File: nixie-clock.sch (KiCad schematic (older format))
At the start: 7 parts

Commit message: Wyprowadzenie VDD (3,3V); komentarze
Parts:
- U?: value STM32F103CBTx -> STM32F103CBT6
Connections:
- net labels added: VDD
- wire segments 13 -> 28
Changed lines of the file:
@@
 P 6000 3850
 F 0 "U?" H 3200 5575 50  0000 L BNN
-F 1 "STM32F103CBTx" H 8800 5575 50  0000 R BNN
+F 1 "STM32F103CBT6" H 8800 5575 50  0000 R BNN
 F 2 "LQFP48" H 8800 5525 50  0000 R TNN
 F 3 "" H 6000 3850 50  0000 C CNN
@@
 	1100 3100 1100 3200
 $Sheet
-S 600  600  950  1000
+S 600  750  850  800
 U 5814F4D4
 F0 "Power supply" 60
 F1 "power-supply.sch" 60
+F2 "VDD" O R 1450 850 60
+F3 "GND" O R 1450 1150 60
+F4 "200VDC" O R 1450 1300 60
+F5 "200VGND" O R 1450 1450 60
+F6 "5VDC" O R 1450 1000 60
 $EndSheet
+$Comp
+L PWR_FLAG #FLG?
+U 1 1 581749DC
+P 1800 700
+F 0 "#FLG?" H 1800 795 50  0001 C CNN
+F 1 "PWR_FLAG" H 1800 880 50  0000 C CNN
+F 2 "" H 1800 700 50  0000 C CNN
+F 3 "" H 1800 700 50  0000 C CNN
+	1    1800 700
+	1    0    0    -1
+$EndComp
+$Comp
+L PWR_FLAG #FLG?
+U 1 1 58174A1B
+P 2250 700
+F 0 "#FLG?" H 2250 795 50  0001 C CNN
+F 1 "PWR_FLAG" H 2250 880 50  0000 C CNN
+F 2 "" H 2250 700 50  0000 C CNN
+F 3 "" H 2250 700 50  0000 C CNN
+	1    2250 700
+	1    0    0    -1
+$EndComp
+Wire Wire Line
+	2250 700  2250 1150
+Wire Wire Line
+	1800 700  1800 850
+Connection ~ 1800 850
+Wire Wire Line
+	2250 1150 1450 1150
+Wire Wire Line
+	1100 2000 1100 2150
+Wire Wire Line
+	1800 850  1450 850
+Text Label 1650 850  2    60   ~ 0
+VDD
+Text Label 1650 1150 2    60   ~ 0
+GND
+Wire Wire Line
+	5600 1900 6100 1900
+Wire Wire Line
+	5800 1900 5800 2050
+Wire Wire Line
+	5900 1900 5900 2050
+Connection ~ 5800 1900
+Wire Wire Line
+	6000 1900 6000 2050
+Connection ~ 5900 1900
+Wire Wire Line
+	6100 1900 6100 2050
+Connection ~ 6000 1900
+Text Label 5750 1900 2    60   ~ 0
+VDD
+Wire Wire Line
+	5600 5800 6100 5800
+Wire Wire Line
+	5800 5800 5800 5650
+Wire Wire Line
+	5900 5800 5900 5650
+Connection ~ 5800 5800
+Wire Wire Line
+	6000 5800 6000 5650
+Connection ~ 5900 5800
+Wire Wire Line
+	6100 5800 6100 5650
+Connection ~ 6000 5800
+Text Label 5750 5800 2    60   ~ 0
+VDD
 $EndSCHEMATC

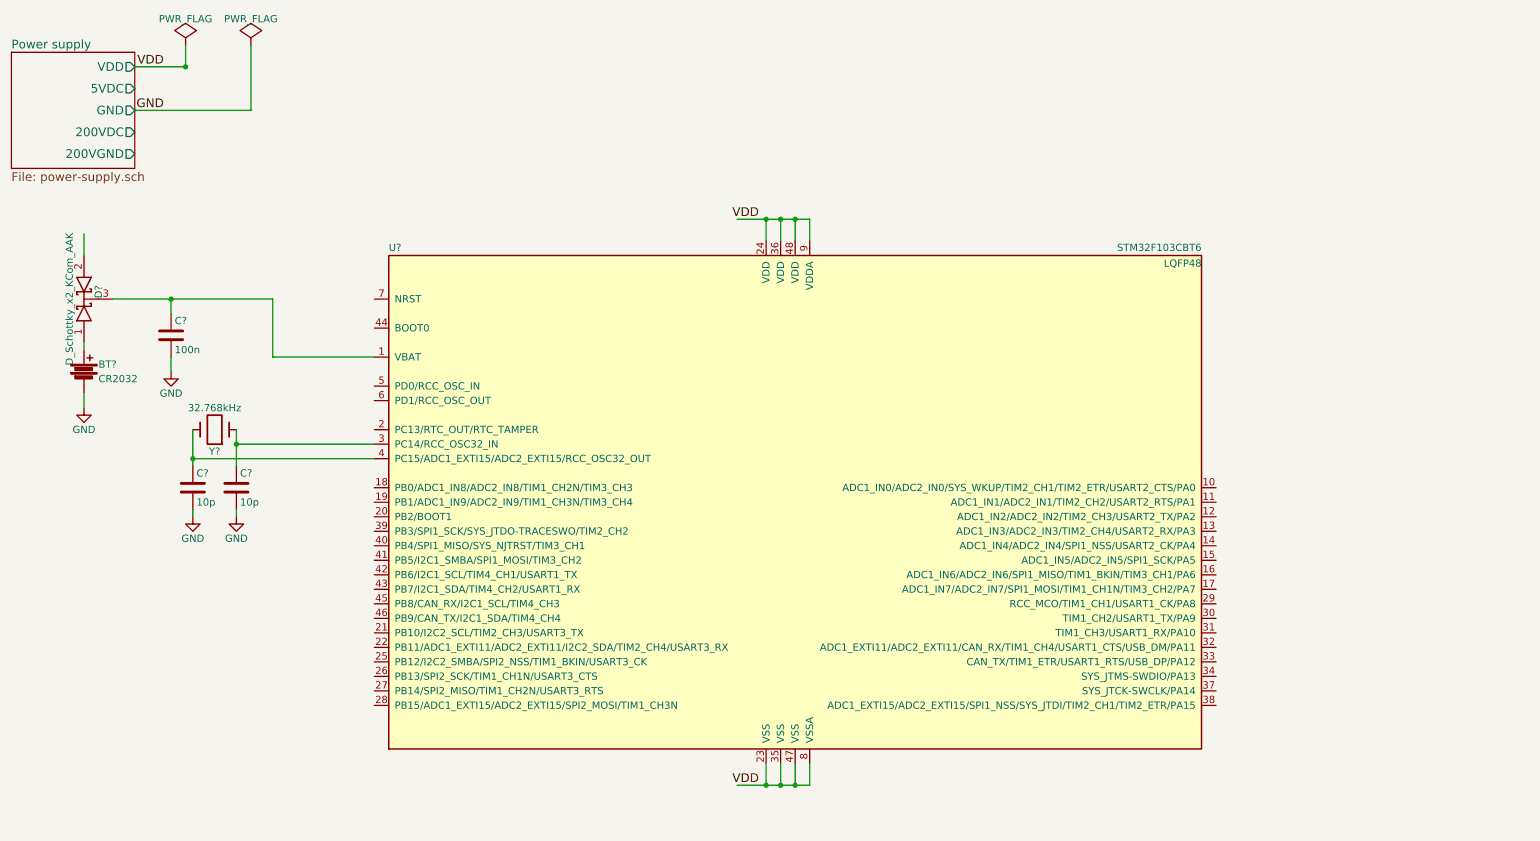
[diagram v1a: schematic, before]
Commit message: Wyprowadzenia do modulu ESP8266
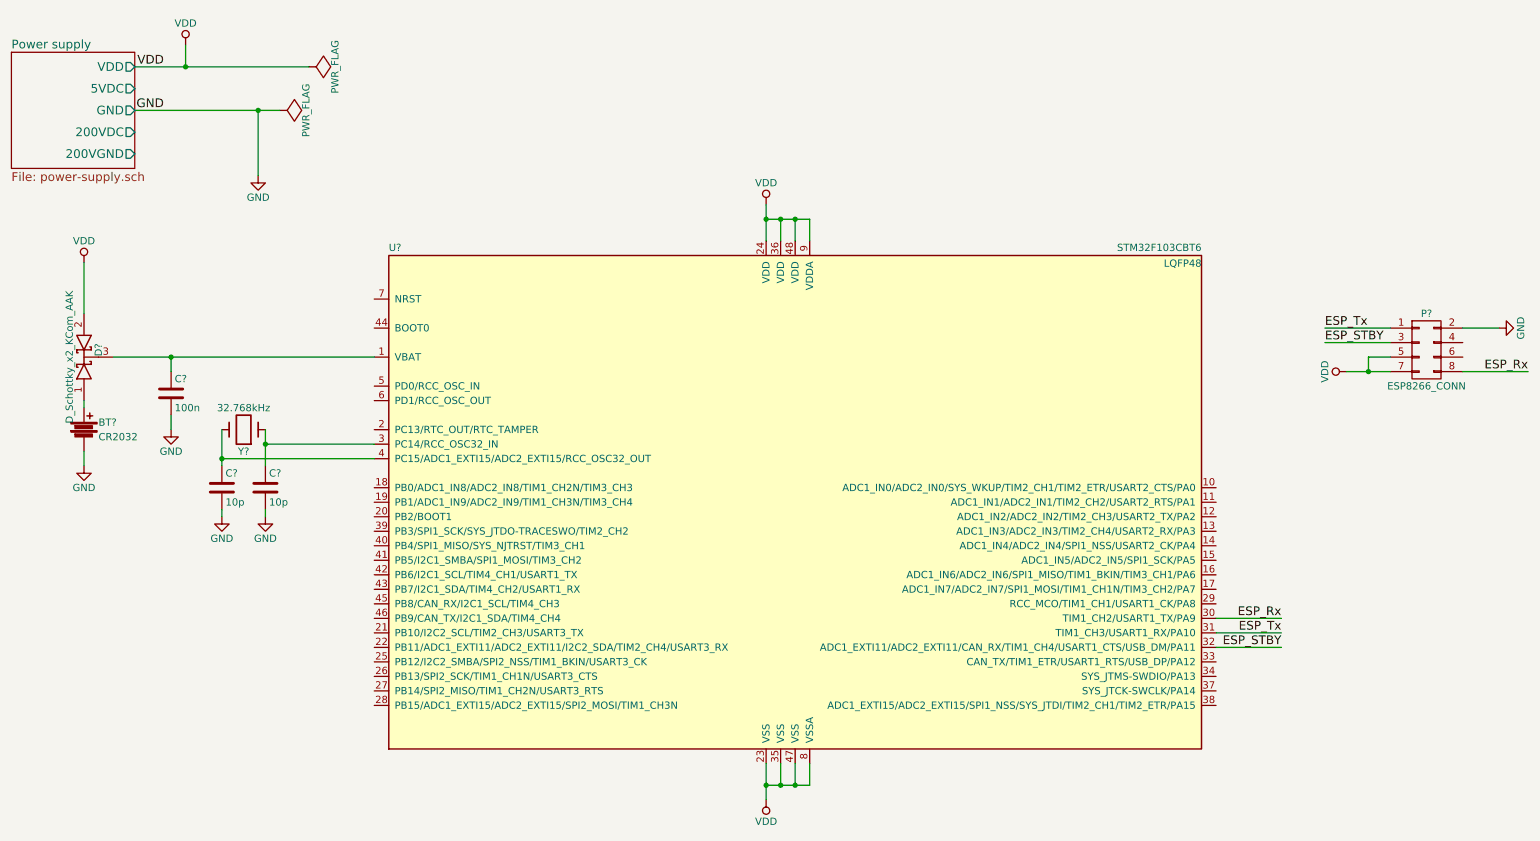
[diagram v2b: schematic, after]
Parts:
- added P?: ESP8266_CONN, symbol CONN_02X04
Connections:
- net labels added: ESP_Rx, ESP_STBY, ESP_Tx
- wire segments 28 -> 48
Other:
- moved on the sheet: BT?, C?, D?, Y?

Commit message: Kontrola jasnosci NIXIE
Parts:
- added RV?: 10k, symbol POT
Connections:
- net GND: now also RV?.1
- net VDD: now also RV?.3
- net BRIGHT_POT: now reaches U?.11 (ADC1_IN1/ADC2_IN1/TIM2_CH2/USART2_RTS/PA1)
- net BRIGHT_POT: now also RV?.2
- net BRIGHT_PWM: now reaches U?.29 (RCC_MCO/TIM1_CH1/USART1_CK/PA8)
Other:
- note added: "Zamienić na EXTI?"
- moved on the sheet: P?
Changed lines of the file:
@@
 $EndComp
 Wire Wire Line
-	2350 3350 2350 3450
-Wire Wire Line
-	2350 3450 2350 3600
+	2350 3350 2350 3600
 Wire Wire Line
 	2350 3450 3100 3450
 Wire Wire Line
-	2050 3350 2050 3550
-Wire Wire Line
-	2050 3550 2050 3600
+	2050 3350 2050 3600
 Wire Wire Line
 	2050 3550 3100 3550
@@
 $EndComp
 Wire Wire Line
-	1300 2850 1700 2850
-Wire Wire Line
-	1700 2850 3100 2850
+	1300 2850 3100 2850
 Wire Wire Line
 	1700 2950 1700 2850
@@
 	1100 3500 1100 3600
 $Sheet
-S 600  750  850  800
+S 1500 750  1150 750
 U 5814F4D4
 F0 "Power supply" 60
 F1 "power-supply.sch" 60
-F2 "VDD" O R 1450 850 60
-F3 "GND" O R 1450 1150 60
-F4 "200VDC" O R 1450 1300 60
-F5 "200VGND" O R 1450 1450 60
-F6 "5VDC" O R 1450 1000 60
+F2 "VDD" O R 2650 850 60
+F3 "GND" O R 2650 1150 60
+F4 "200VDC" O R 2650 1300 60
+F5 "200VGND" O R 2650 1450 60
+F6 "5VDC" O R 2650 1000 60
+F7 "BRIGHT_PWM" I L 1500 850 60
 $EndSheet
 $Comp
 L PWR_FLAG #FLG?
 U 1 1 581749DC
-P 2650 850
-F 0 "#FLG?" H 2650 945 50  0001 C CNN
-F 1 "PWR_FLAG" H 2650 1030 50  0000 C CNN
-F 2 "" H 2650 850 50  0000 C CNN
-F 3 "" H 2650 850 50  0000 C CNN
-	1    2650 850
+P 3850 850
+F 0 "#FLG?" H 3850 945 50  0001 C CNN
+F 1 "PWR_FLAG" H 3850 1030 50  0000 C CNN
+F 2 "" H 3850 850 50  0000 C CNN
+F 3 "" H 3850 850 50  0000 C CNN
+	1    3850 850
 	0    1    1    0
 $EndComp
@@
 L PWR_FLAG #FLG?
 U 1 1 58174A1B
-P 2450 1150
-F 0 "#FLG?" H 2450 1245 50  0001 C CNN
-F 1 "PWR_FLAG" H 2450 1330 50  0000 C CNN
-F 2 "" H 2450 1150 50  0000 C CNN
-F 3 "" H 2450 1150 50  0000 C CNN
-	1    2450 1150
+P 3650 1150
+F 0 "#FLG?" H 3650 1245 50  0001 C CNN
+F 1 "PWR_FLAG" H 3650 1330 50  0000 C CNN
+F 2 "" H 3650 1150 50  0000 C CNN
+F 3 "" H 3650 1150 50  0000 C CNN
+	1    3650 1150
 	0    1    1    0
 $EndComp
 Wire Wire Line
-	1450 1150 2300 1150
-Wire Wire Line
-	2300 1150 2450 1150
-Wire Wire Line
-	2300 1150 2300 1600
-Wire Wire Line
-	1800 700  1800 850
+	2650 1150 3650 1150
+Wire Wire Line
+	3500 1150 3500 1600
+Wire Wire Line
+	3000 700  3000 850
 Wire Wire Line
 	1100 2200 1100 2550
 Wire Wire Line
-	1450 850  1800 850
-Wire Wire Line
-	1800 850  2650 850
-Text Label 1650 850  2    60   ~ 0
+	2650 850  3850 850
+Text Label 2850 850  2    60   ~ 0
 VDD
-Text Label 1650 1150 2    60   ~ 0
+Text Label 2850 1150 2    60   ~ 0
 GND
 Wire Wire Line
-	5800 1800 5800 1900
-Wire Wire Line
-	5800 1900 5800 2050
-Wire Wire Line
-	5800 1900 5900 1900
-Wire Wire Line
-	5900 1900 6000 1900
-Wire Wire Line
-	6000 1900 6100 1900
+	5800 1800 5800 2050
+Wire Wire Line
+	5800 1900 6100 1900
 Wire Wire Line
 	5900 1900 5900 2050
@@
 Connection ~ 6000 1900
 Wire Wire Line
-	5800 5650 5800 5800
-Wire Wire Line
-	5800 5800 5800 5900
-Wire Wire Line
-	5800 5800 5900 5800
-Wire Wire Line
-	5900 5800 6000 5800
-Wire Wire Line
-	6000 5800 6100 5800
+	5800 5650 5800 5900
+Wire Wire Line
+	5800 5800 6100 5800
 Wire Wire Line
 	5900 5800 5900 5650
@@
 L GND #PWR?
 U 1 1 58173306
-P 2300 1600
-F 0 "#PWR?" H 2300 1350 50  0001 C CNN
-F 1 "GND" H 2300 1450 50  0000 C CNN
-F 2 "" H 2300 1600 50  0000 C CNN
-F 3 "" H 2300 1600 50  0000 C CNN
-	1    2300 1600
-	1    0    0    -1
-$EndComp
-Connection ~ 2300 1150
+P 3500 1600
+F 0 "#PWR?" H 3500 1350 50  0001 C CNN
+F 1 "GND" H 3500 1450 50  0000 C CNN
+F 2 "" H 3500 1600 50  0000 C CNN
+F 3 "" H 3500 1600 50  0000 C CNN
+	1    3500 1600
+	1    0    0    -1
+$EndComp
+Connection ~ 3500 1150
 $Comp
 L VDD #PWR?
 U 1 1 58175A0D
-P 1800 700
-F 0 "#PWR?" H 1800 550 50  0001 C CNN
-F 1 "VDD" H 1800 850 50  0000 C CNN
-F 2 "" H 1800 700 50  0000 C CNN
-F 3 "" H 1800 700 50  0000 C CNN
-	1    1800 700
+P 3000 700
+F 0 "#PWR?" H 3000 550 50  0001 C CNN
+F 1 "VDD" H 3000 850 50  0000 C CNN
+F 2 "" H 3000 700 50  0000 C CNN
+F 3 "" H 3000 700 50  0000 C CNN
+	1    3000 700
 	1    0    0    -1
 $EndComp
@@
 	-1   0    0    1
 $EndComp
-Connection ~ 1800 850
+Connection ~ 3000 850
 $Comp
 L CONN_02X04 P?
 U 1 1 5817ACF2
-P 10350 2800
-F 0 "P?" H 10350 3050 50  0000 C CNN
-F 1 "ESP8266_CONN" H 10350 2550 50  0000 C CNN
-F 2 "" H 10350 1600 50  0000 C CNN
-F 3 "" H 10350 1600 50  0000 C CNN
-	1    10350 2800
-	1    0    0    -1
-$EndComp
-Wire Wire Line
-	10600 2650 10850 2650
+P 10350 2200
+F 0 "P?" H 10350 2450 50  0000 C CNN
+F 1 "ESP8266_CONN" H 10350 1950 50  0000 C CNN
+F 2 "" H 10350 1000 50  0000 C CNN
+F 3 "" H 10350 1000 50  0000 C CNN
+	1    10350 2200
+	1    0    0    -1
+$EndComp
+Wire Wire Line
+	10600 2050 10850 2050
 $Comp
 L GND #PWR?
 U 1 1 5817B257
-P 10850 2650
-F 0 "#PWR?" H 10850 2400 50  0001 C CNN
-F 1 "GND" H 10850 2500 50  0000 C CNN
-F 2 "" H 10850 2650 50  0000 C CNN
-F 3 "" H 10850 2650 50  0000 C CNN
-	1    10850 2650
+P 10850 2050
+F 0 "#PWR?" H 10850 1800 50  0001 C CNN
+F 1 "GND" H 10850 1900 50  0000 C CNN
+F 2 "" H 10850 2050 50  0000 C CNN
+F 3 "" H 10850 2050 50  0000 C CNN
+	1    10850 2050
 	0    -1   -1   0
 $EndComp
@@
 L VDD #PWR?
 U 1 1 5817B5C8
-P 9800 2950
-F 0 "#PWR?" H 9800 2800 50  0001 C CNN
-F 1 "VDD" H 9800 3100 50  0000 C CNN
-F 2 "" H 9800 2950 50  0000 C CNN
-F 3 "" H 9800 2950 50  0000 C CNN
-	1    9800 2950
+P 9800 2350
+F 0 "#PWR?" H 9800 2200 50  0001 C CNN
+F 1 "VDD" H 9800 2500 50  0000 C CNN
+F 2 "" H 9800 2350 50  0000 C CNN
+F 3 "" H 9800 2350 50  0000 C CNN
+	1    9800 2350
 	0    -1   -1   0
 $EndComp
 Wire Wire Line
-	9800 2950 9950 2950
-Wire Wire Line
-	9950 2950 10100 2950
-Wire Wire Line
-	9950 2950 9950 2850
-Wire Wire Line
-	9950 2850 10100 2850
-Connection ~ 9950 2950
-Wire Wire Line
-	8900 4650 9350 4650
-Wire Wire Line
-	8900 4750 9350 4750
-Text Label 9350 4650 2    60   ~ 0
+	9800 2350 10100 2350
+Wire Wire Line
+	9950 2350 9950 2250
+Wire Wire Line
+	9950 2250 10100 2250
+Connection ~ 9950 2350
+Wire Wire Line
+	8900 4650 9500 4650
+Wire Wire Line
+	8900 4750 9500 4750
+Text Label 9500 4650 2    60   ~ 0
 ESP_Rx
-Text Label 9350 4750 2    60   ~ 0
+Text Label 9500 4750 2    60   ~ 0
 ESP_Tx
 Wire Wire Line
-	10100 2650 9650 2650
-Text Label 9650 2650 0    60   ~ 0
+	10100 2050 9650 2050
+Text Label 9650 2050 0    60   ~ 0
 ESP_Tx
 Wire Wire Line
-	10600 2950 11050 2950
-Text Label 11050 2950 2    60   ~ 0
+	10600 2350 11050 2350
+Text Label 11050 2350 2    60   ~ 0
 ESP_Rx
 Wire Wire Line
-	8900 4850 9350 4850
-Text Label 9350 4850 2    60   ~ 0
+	8900 4850 9500 4850
+Text Label 9500 4850 2    60   ~ 0
 ESP_STBY
 Wire Wire Line
-	10100 2750 9650 2750
-Text Label 9650 2750 0    60   ~ 0
+	10100 2150 9650 2150
+Text Label 9650 2150 0    60   ~ 0
 ESP_STBY
+Wire Wire Line
+	8900 4550 9500 4550
+Text Label 9500 4550 2    60   ~ 0
+BRIGHT_PWM
+Wire Wire Line
+	1500 850  700  850
+Text Label 700  850  0    60   ~ 0
+BRIGHT_PWM
+$Comp
+L POT RV?
+U 1 1 58181F47
+P 10750 1050
+F 0 "RV?" H 10750 970 50  0000 C CNN
+F 1 "10k" H 10750 1050 50  0000 C CNN
+F 2 "" H 10750 1050 50  0000 C CNN
+F 3 "" H 10750 1050 50  0000 C CNN
+	1    10750 1050
+	0    -1   -1   0
+$EndComp
+Wire Wire Line
+	10750 900  10750 800
+Wire Wire Line
+	10750 1200 10750 1300
+$Comp
+L VDD #PWR?
+U 1 1 58182C82
+P 10750 800
+F 0 "#PWR?" H 10750 650 50  0001 C CNN
+F 1 "VDD" H 10750 950 50  0000 C CNN
+F 2 "" H 10750 800 50  0000 C CNN
+F 3 "" H 10750 800 50  0000 C CNN
+	1    10750 800
+	1    0    0    -1
+$EndComp
+$Comp
+L GND #PWR?
+U 1 1 58182F5B
+P 10750 1300
+F 0 "#PWR?" H 10750 1050 50  0001 C CNN
+F 1 "GND" H 10750 1150 50  0000 C CNN
+F 2 "" H 10750 1300 50  0000 C CNN
+F 3 "" H 10750 1300 50  0000 C CNN
+	1    10750 1300
+	1    0    0    -1
+$EndComp
+Wire Wire Line
+	10600 1050 9950 1050
+Text Label 9950 1050 0    60   ~ 0
+BRIGHT_POT
+Wire Wire Line
+	8900 3850 9500 3850
+Text Label 9500 3850 2    60   ~ 0
+BRIGHT_POT
+Text Notes 9600 3850 0    60   ~ 0
+Zamienić na EXTI?
 $EndSCHEMATC
